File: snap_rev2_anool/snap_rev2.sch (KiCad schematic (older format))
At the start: 30 parts, among them J1 SJ2-35863B1, P1 CONN_02X05, Q1 TSM2301, SW1 1825910-6, U1 TPS610986, U2 MDBT42Q, Y1 32786Hz

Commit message: changed RGB LED fp
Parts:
- D1: footprint snap_fp:LED_RGB_PLCC-6 -> snap_fp:LED_RGB_5050-6
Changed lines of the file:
@@
-EESchema Schematic File Version 3
+EESchema Schematic File Version 2
 LIBS:snap_rev2_symbol
 LIBS:power
@@
 LIBS:audio-jack-4_1switches
 LIBS:snap_rev2-cache
-EELAYER 26 0
+EELAYER 25 0
 EELAYER END
 $Descr A4 11693 8268
@@
 F 0 "D1" H 6825 825 50  0000 C CNN
 F 1 "CLX6F-FKC" H 6825 1581 50  0000 C CNN
-F 2 "snap_fp:LED_RGB_PLCC-6" H 6825 1125 50  0001 C CNN
+F 2 "snap_fp:LED_RGB_5050-6" H 6825 1125 50  0001 C CNN
 F 3 "http://www.cree.com/led-components/media/documents/ds-CLX6F-FKC-1352.pdf" H 6825 1125 50  0001 C CNN
 F 4 "CLX6F-FKC" H 0   0   60  0001 C CNN "Part Number"

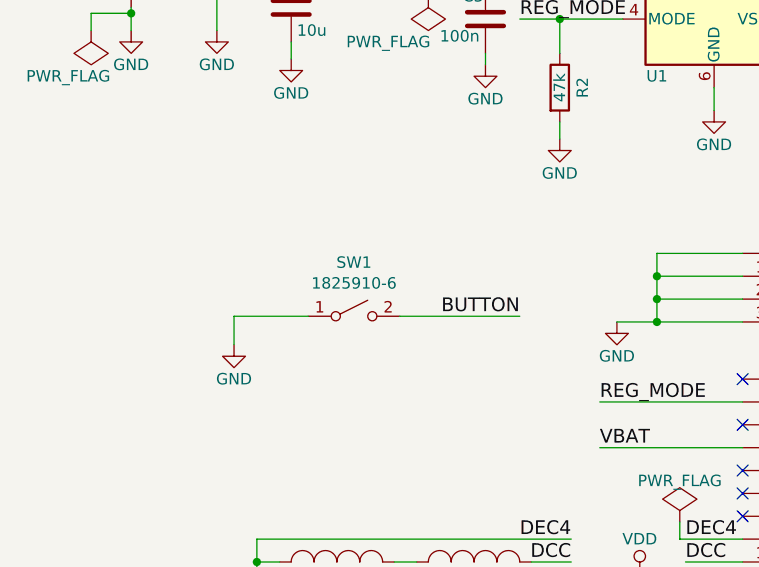
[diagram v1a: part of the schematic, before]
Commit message: added SMD switch 3D model
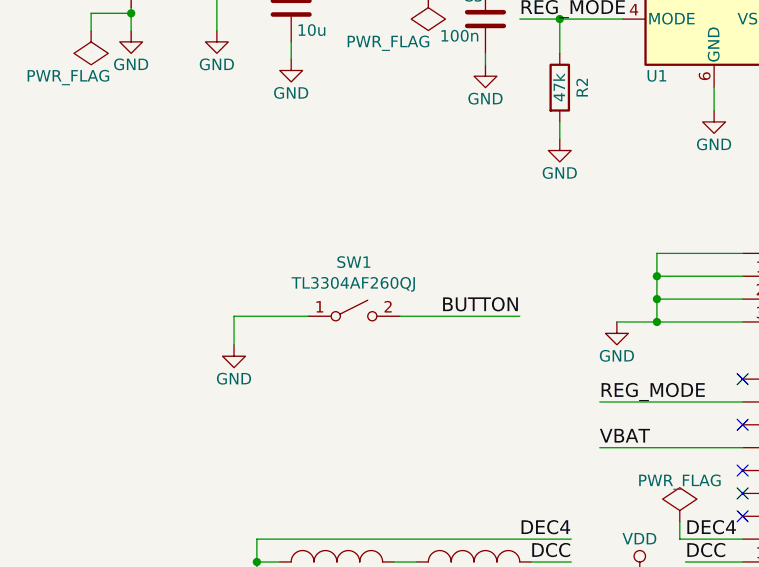
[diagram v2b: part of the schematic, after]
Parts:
- D1, Y1: manf# (none) -> Value
- SW1: value 1825910-6 -> TL3304AF260QJ; manf# (none) -> Value
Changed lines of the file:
@@
-EESchema Schematic File Version 2
+EESchema Schematic File Version 3
 LIBS:snap_rev2_symbol
 LIBS:power
@@
 LIBS:audio-jack-4_1switches
 LIBS:snap_rev2-cache
-EELAYER 25 0
+EELAYER 26 0
 EELAYER END
 $Descr A4 11693 8268
@@
 F 1 "CLX6F-FKC" H 6825 1581 50  0000 C CNN
 F 2 "snap_fp:LED_RGB_5050-6" H 6825 1125 50  0001 C CNN
-F 3 "http://www.cree.com/led-components/media/documents/ds-CLX6F-FKC-1352.pdf" H 6825 1125 50  0001 C CNN
-F 4 "CLX6F-FKC" H 0   0   60  0001 C CNN "Part Number"
+F 3 "https://d114hh0cykhyb0.cloudfront.net/pdfs/5050-RGB.pdf" H 6825 1125 50  0001 C CNN
+F 4 "Value" H 6825 1175 60  0001 C CNN "manf#"
+F 5 "CLX6F-FKC" H 0   0   60  0001 C CNN "Part Number"
 	1    6825 1175
 	1    0    0    -1
@@
 P 3200 2725
 F 0 "SW1" H 3200 2960 50  0000 C CNN
-F 1 "1825910-6" H 3200 2869 50  0000 C CNN
+F 1 "TL3304AF260QJ" H 3200 2869 50  0000 C CNN
 F 2 "snap_fp:SW_SPST_B3SL-1002P" H 3200 2725 50  0001 C CNN
-F 3 "http://www.te.com/commerce/DocumentDelivery/DDEController?Action=srchrtrv&DocNm=1825910&DocType=Customer+Drawing&DocLang=English" H 3200 2725 50  0001 C CNN
+F 3 "https://www.digikey.com/product-detail/en/e-switch/TL3304AF260QJ/EG4377TR-ND/1144802" H 3200 2725 50  0001 C CNN
+F 4 "Value" H 3200 2725 60  0001 C CNN "manf#"
 	1    3200 2725
 	1    0    0    -1
@@
 F 1 "32786Hz" H 5025 5450 50  0000 C CNN
 F 2 "snap_fp:Crystal_C38-LF_d3.0mm_l8.0mm_Horizontal" H 5025 5600 50  0001 C CNN
-F 3 "http://cfd.citizen.co.jp/english/prod-tech/product/pdf/datasheet_TF/CFS-206_CFS-145_E.pdf" H 5025 5600 50  0001 C CNN
+F 3 "https://www.ecsxtal.com/store/pdf/ECS-3x8X%202x6X%201X5X.pdf" H 5025 5600 50  0001 C CNN
+F 4 "Value" H 5025 5600 60  0001 C CNN "manf#"
 	1    5025 5600
 	-1   0    0    1
